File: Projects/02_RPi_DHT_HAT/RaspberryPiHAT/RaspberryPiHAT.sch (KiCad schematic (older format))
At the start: 0 parts

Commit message: Project 2: Add symbols from parts.md to Eeschema
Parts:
- added D?: D, symbol Device:D
- added J?: Raspberry_Pi_2_3, symbol Connector:Raspberry_Pi_2_3
- added R? (x3): R, symbol Device:R
- added SW?: SW_DPST, symbol Switch:SW_DPST
- added U?: DHT22, Sensor:Aosong_DHT11_5.5x12.0_P2.54mm, symbol Sensor:DHT11
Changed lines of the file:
@@
 Comment4 ""
 $EndDescr
+$Comp
+L Connector:Raspberry_Pi_2_3 J?
+U 1 1 61CF6995
+P 5550 3750
+F 0 "J?" H 5550 5231 50  0000 C CNN
+F 1 "Raspberry_Pi_2_3" H 5550 5140 50  0000 C CNN
+F 2 "" H 5550 3750 50  0001 C CNN
+F 3 "https://www.raspberrypi.org/documentation/hardware/raspberrypi/schematics/rpi_SCH_3bplus_1p0_reduced.pdf" H 5550 3750 50  0001 C CNN
+	1    5550 3750
+	1    0    0    -1
+$EndComp
+$Comp
+L Device:R R?
+U 1 1 61CFAE04
+P 3850 3000
+F 0 "R?" H 3920 3046 50  0000 L CNN
+F 1 "R" H 3920 2955 50  0000 L CNN
+F 2 "" V 3780 3000 50  0001 C CNN
+F 3 "~" H 3850 3000 50  0001 C CNN
+	1    3850 3000
+	1    0    0    -1
+$EndComp
+$Comp
+L Device:R R?
+U 1 1 61CFD123
+P 3850 3450
+F 0 "R?" H 3920 3496 50  0000 L CNN
+F 1 "R" H 3920 3405 50  0000 L CNN
+F 2 "" V 3780 3450 50  0001 C CNN
+F 3 "~" H 3850 3450 50  0001 C CNN
+	1    3850 3450
+	1    0    0    -1
+$EndComp
+$Comp
+L Sensor:DHT11 U?
+U 1 1 61CFDA18
+P 3850 4250
+F 0 "U?" H 3606 4296 50  0000 R CNN
+F 1 "DHT22" H 3606 4205 50  0000 R CNN
+F 2 "Sensor:Aosong_DHT11_5.5x12.0_P2.54mm" H 3850 3850 50  0001 C CNN
+F 3 "http://akizukidenshi.com/download/ds/aosong/DHT11.pdf" H 4000 4500 50  0001 C CNN
+	1    3850 4250
+	1    0    0    -1
+$EndComp
+$Comp
+L Device:D D?
+U 1 1 61CFE829
+P 3850 2450
+F 0 "D?" H 3850 2667 50  0000 C CNN
+F 1 "D" H 3850 2576 50  0000 C CNN
+F 2 "" H 3850 2450 50  0001 C CNN
+F 3 "~" H 3850 2450 50  0001 C CNN
+	1    3850 2450
+	1    0    0    -1
+$EndComp
+$Comp
+L Device:R R?
+U 1 1 61CFF65D
+P 7350 3550
+F 0 "R?" H 7420 3596 50  0000 L CNN
+F 1 "R" H 7420 3505 50  0000 L CNN
+F 2 "" V 7280 3550 50  0001 C CNN
+F 3 "~" H 7350 3550 50  0001 C CNN
+	1    7350 3550
+	1    0    0    -1
+$EndComp
+$Comp
+L Switch:SW_DPST SW?
+U 1 1 61D01499
+P 7350 2900
+F 0 "SW?" H 7350 3225 50  0000 C CNN
+F 1 "SW_DPST" H 7350 3134 50  0000 C CNN
+F 2 "" H 7350 2900 50  0001 C CNN
+F 3 "~" H 7350 2900 50  0001 C CNN
+	1    7350 2900
+	1    0    0    -1
+$EndComp
 $EndSCHEMATC

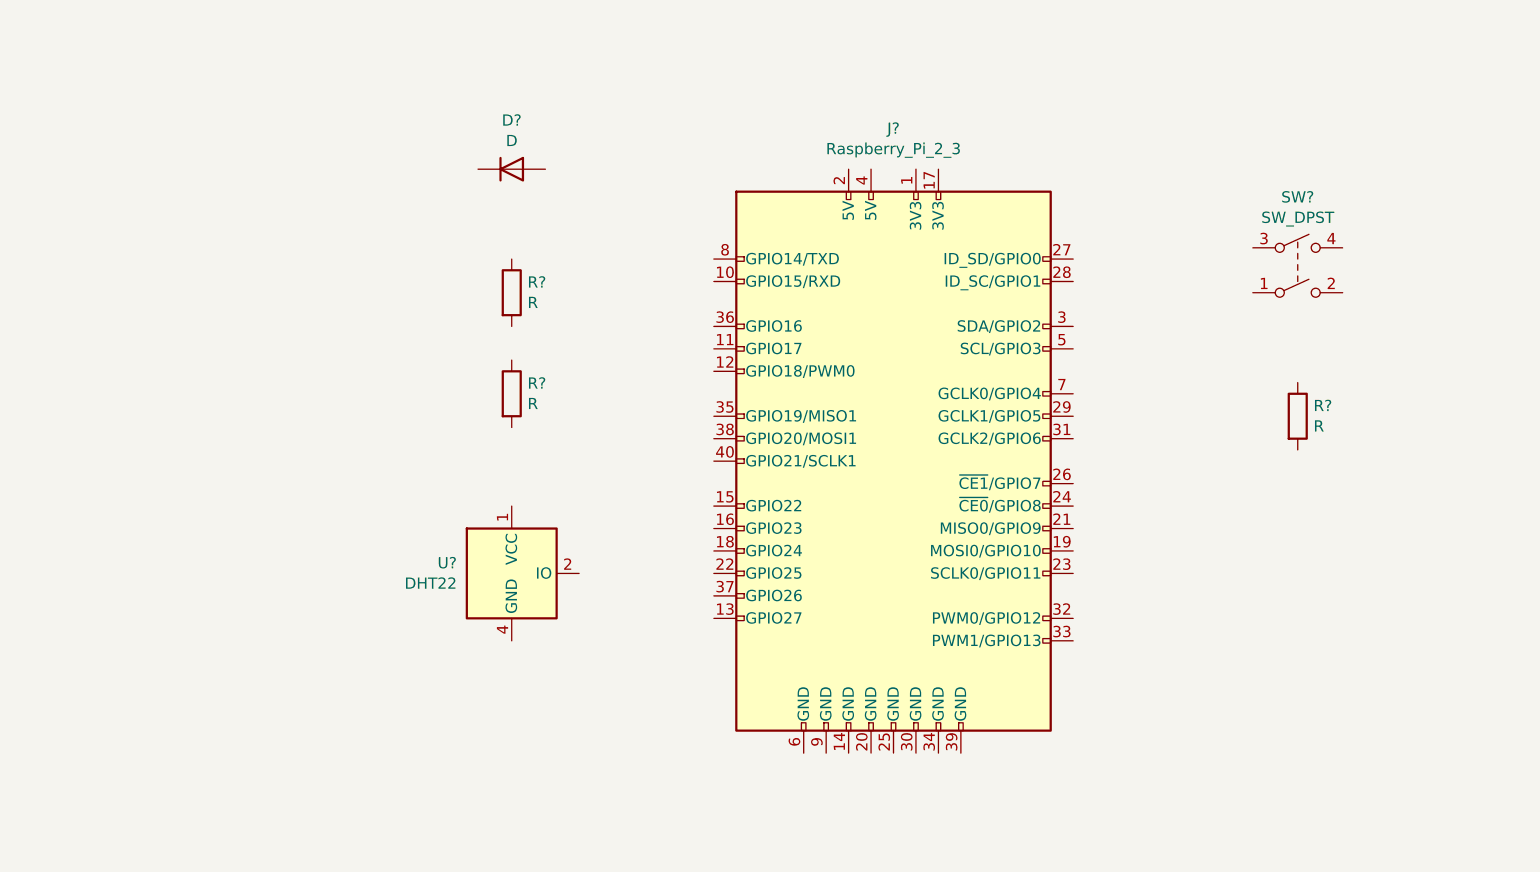
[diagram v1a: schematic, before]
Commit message: Project 2: Arrange, annotate, and associate Eeschema with footprints
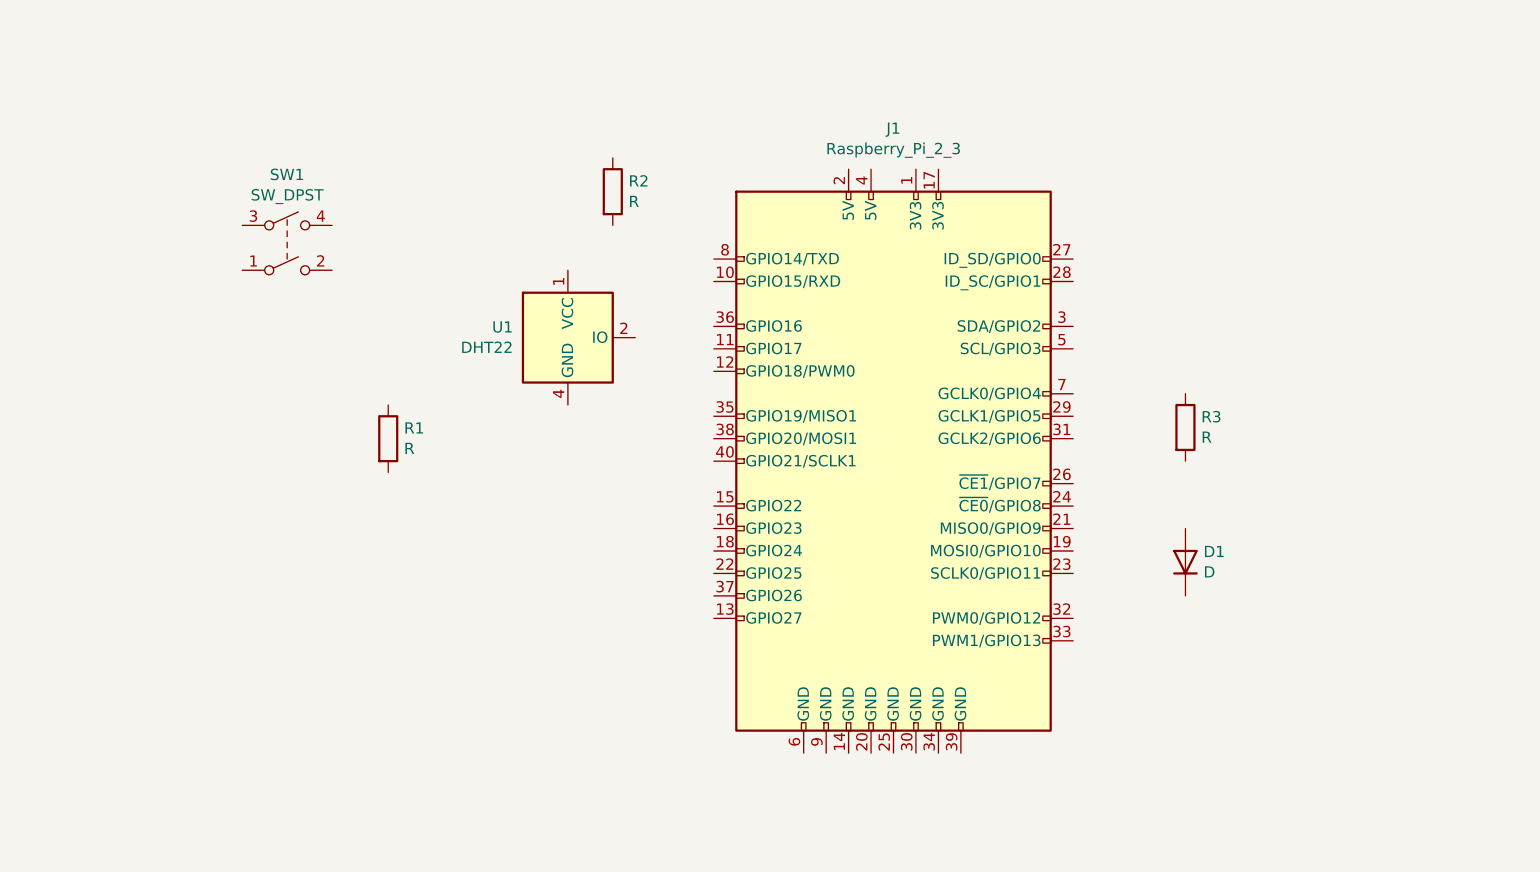
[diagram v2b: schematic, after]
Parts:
- D1: renamed from D?; footprint (none) -> LED_SMD:LED_0805_2012Metric
- J1: renamed from J?; footprint (none) -> Connector_PinSocket_2.54mm:PinSocket_2x08_P2.54mm_Vertical
- R1, R2, R3: renamed from R?; footprint (none) -> Resistor_SMD:R_0805_2012Metric
- SW1: renamed from SW?; footprint (none) -> freetronics_footprints:SW_PUSHBUTTON_PTH
- gave numbers to parts that had none: 1
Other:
- moved on the sheet: D1, R1, R2, R3, SW1, U1
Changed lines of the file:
@@
 $EndDescr
 $Comp
-L Connector:Raspberry_Pi_2_3 J?
+L Connector:Raspberry_Pi_2_3 J1
 U 1 1 61CF6995
 P 5550 3750
-F 0 "J?" H 5550 5231 50  0000 C CNN
+F 0 "J1" H 5550 5231 50  0000 C CNN
 F 1 "Raspberry_Pi_2_3" H 5550 5140 50  0000 C CNN
-F 2 "" H 5550 3750 50  0001 C CNN
+F 2 "Connector_PinSocket_2.54mm:PinSocket_2x08_P2.54mm_Vertical" H 5550 3750 50  0001 C CNN
 F 3 "https://www.raspberrypi.org/documentation/hardware/raspberrypi/schematics/rpi_SCH_3bplus_1p0_reduced.pdf" H 5550 3750 50  0001 C CNN
 	1    5550 3750
@@
 $EndComp
 $Comp
-L Device:R R?
+L Device:R R2
 U 1 1 61CFAE04
-P 3850 3000
-F 0 "R?" H 3920 3046 50  0000 L CNN
-F 1 "R" H 3920 2955 50  0000 L CNN
-F 2 "" V 3780 3000 50  0001 C CNN
-F 3 "~" H 3850 3000 50  0001 C CNN
-	1    3850 3000
+P 4300 2550
+F 0 "R2" H 4370 2596 50  0000 L CNN
+F 1 "R" H 4370 2505 50  0000 L CNN
+F 2 "Resistor_SMD:R_0805_2012Metric" V 4230 2550 50  0001 C CNN
+F 3 "~" H 4300 2550 50  0001 C CNN
+	1    4300 2550
 	1    0    0    -1
 $EndComp
 $Comp
-L Device:R R?
+L Device:R R3
 U 1 1 61CFD123
-P 3850 3450
-F 0 "R?" H 3920 3496 50  0000 L CNN
-F 1 "R" H 3920 3405 50  0000 L CNN
-F 2 "" V 3780 3450 50  0001 C CNN
-F 3 "~" H 3850 3450 50  0001 C CNN
-	1    3850 3450
+P 6850 3600
+F 0 "R3" H 6920 3646 50  0000 L CNN
+F 1 "R" H 6920 3555 50  0000 L CNN
+F 2 "Resistor_SMD:R_0805_2012Metric" V 6780 3600 50  0001 C CNN
+F 3 "~" H 6850 3600 50  0001 C CNN
+	1    6850 3600
 	1    0    0    -1
 $EndComp
 $Comp
-L Sensor:DHT11 U?
+L Sensor:DHT11 U1
 U 1 1 61CFDA18
-P 3850 4250
-F 0 "U?" H 3606 4296 50  0000 R CNN
-F 1 "DHT22" H 3606 4205 50  0000 R CNN
-F 2 "Sensor:Aosong_DHT11_5.5x12.0_P2.54mm" H 3850 3850 50  0001 C CNN
-F 3 "http://akizukidenshi.com/download/ds/aosong/DHT11.pdf" H 4000 4500 50  0001 C CNN
-	1    3850 4250
+P 4100 3200
+F 0 "U1" H 3856 3246 50  0000 R CNN
+F 1 "DHT22" H 3856 3155 50  0000 R CNN
+F 2 "Sensor:Aosong_DHT11_5.5x12.0_P2.54mm" H 4100 2800 50  0001 C CNN
+F 3 "http://akizukidenshi.com/download/ds/aosong/DHT11.pdf" H 4250 3450 50  0001 C CNN
+	1    4100 3200
 	1    0    0    -1
 $EndComp
 $Comp
-L Device:D D?
+L Device:D D1
 U 1 1 61CFE829
-P 3850 2450
-F 0 "D?" H 3850 2667 50  0000 C CNN
-F 1 "D" H 3850 2576 50  0000 C CNN
-F 2 "" H 3850 2450 50  0001 C CNN
-F 3 "~" H 3850 2450 50  0001 C CNN
-	1    3850 2450
+P 6850 4200
+F 0 "D1" V 6896 4120 50  0000 R CNN
+F 1 "D" V 6805 4120 50  0000 R CNN
+F 2 "LED_SMD:LED_0805_2012Metric" H 6850 4200 50  0001 C CNN
+F 3 "~" H 6850 4200 50  0001 C CNN
+	1    6850 4200
+	0    -1   -1   0
+$EndComp
+$Comp
+L Device:R R1
+U 1 1 61CFF65D
+P 3300 3650
+F 0 "R1" H 3370 3696 50  0000 L CNN
+F 1 "R" H 3370 3605 50  0000 L CNN
+F 2 "Resistor_SMD:R_0805_2012Metric" V 3230 3650 50  0001 C CNN
+F 3 "~" H 3300 3650 50  0001 C CNN
+	1    3300 3650
 	1    0    0    -1
 $EndComp
 $Comp
-L Device:R R?
-U 1 1 61CFF65D
-P 7350 3550
-F 0 "R?" H 7420 3596 50  0000 L CNN
-F 1 "R" H 7420 3505 50  0000 L CNN
-F 2 "" V 7280 3550 50  0001 C CNN
-F 3 "~" H 7350 3550 50  0001 C CNN
-	1    7350 3550
+L Switch:SW_DPST SW1
+U 1 1 61D01499
+P 2850 2800
+F 0 "SW1" H 2850 3125 50  0000 C CNN
+F 1 "SW_DPST" H 2850 3034 50  0000 C CNN
+F 2 "freetronics_footprints:SW_PUSHBUTTON_PTH" H 2850 2800 50  0001 C CNN
+F 3 "~" H 2850 2800 50  0001 C CNN
+	1    2850 2800
 	1    0    0    -1
 $EndComp
-$Comp
-L Switch:SW_DPST SW?
-U 1 1 61D01499
-P 7350 2900
-F 0 "SW?" H 7350 3225 50  0000 C CNN
-F 1 "SW_DPST" H 7350 3134 50  0000 C CNN
-F 2 "" H 7350 2900 50  0001 C CNN
-F 3 "~" H 7350 2900 50  0001 C CNN
-	1    7350 2900
-	1    0    0    -1
-$EndComp

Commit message: Project 2: Wire signals and power (PWR_FLAG)
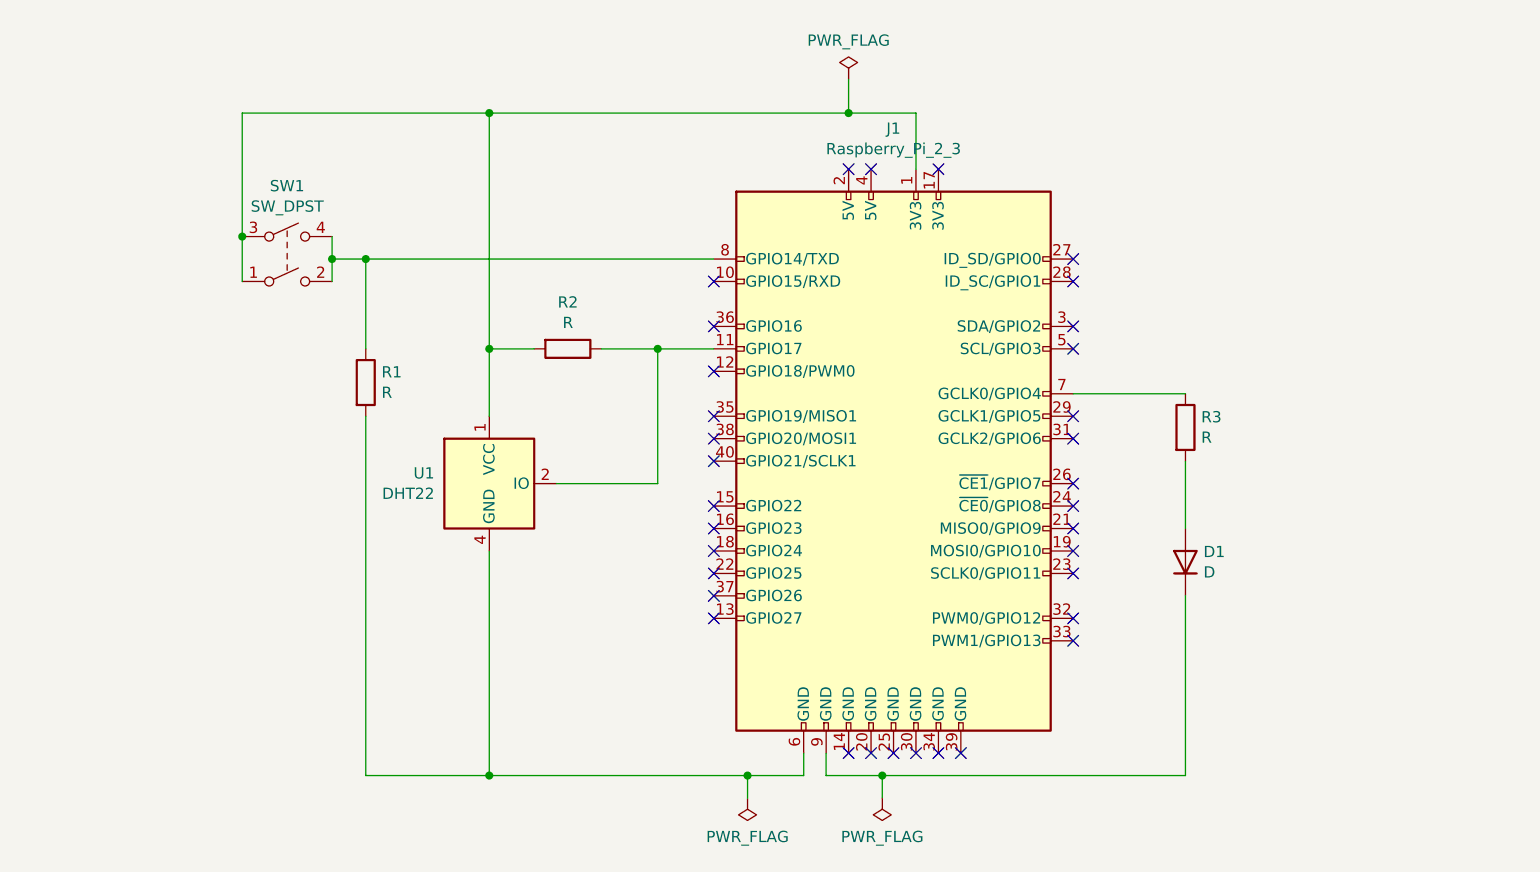
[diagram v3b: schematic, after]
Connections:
- net at J1.1 (3V3): now also R2.2, SW1.1, SW1.3, U1.1 (VCC)
- net at J1.11 (GPIO17): now also R2.1, U1.2 (IO)
- net at J1.6 (GND): now also R1.2, U1.4 (GND)
- net at J1.7 (GCLK0/GPIO4): now also R3.1
- net at J1.8 (GPIO14/TXD): now also R1.1, SW1.2, SW1.4
- net at J1.9 (GND): now also D1.1 (K)
- net at R3.2: now also D1.2 (A)
- no-connect marks 0 -> 34
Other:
- moved on the sheet: R1, R2, SW1, U1
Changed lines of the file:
@@
 $EndDescr
-$Comp
-L Connector:Raspberry_Pi_2_3 J1
-U 1 1 61CF6995
-P 5550 3750
-F 0 "J1" H 5550 5231 50  0000 C CNN
-F 1 "Raspberry_Pi_2_3" H 5550 5140 50  0000 C CNN
-F 2 "Connector_PinSocket_2.54mm:PinSocket_2x08_P2.54mm_Vertical" H 5550 3750 50  0001 C CNN
-F 3 "https://www.raspberrypi.org/documentation/hardware/raspberrypi/schematics/rpi_SCH_3bplus_1p0_reduced.pdf" H 5550 3750 50  0001 C CNN
-	1    5550 3750
-	1    0    0    -1
-$EndComp
-$Comp
-L Device:R R2
-U 1 1 61CFAE04
-P 4300 2550
-F 0 "R2" H 4370 2596 50  0000 L CNN
-F 1 "R" H 4370 2505 50  0000 L CNN
-F 2 "Resistor_SMD:R_0805_2012Metric" V 4230 2550 50  0001 C CNN
-F 3 "~" H 4300 2550 50  0001 C CNN
-	1    4300 2550
-	1    0    0    -1
-$EndComp
 $Comp
 L Device:R R3
@@
 L Sensor:DHT11 U1
 U 1 1 61CFDA18
-P 4100 3200
-F 0 "U1" H 3856 3246 50  0000 R CNN
-F 1 "DHT22" H 3856 3155 50  0000 R CNN
-F 2 "Sensor:Aosong_DHT11_5.5x12.0_P2.54mm" H 4100 2800 50  0001 C CNN
-F 3 "http://akizukidenshi.com/download/ds/aosong/DHT11.pdf" H 4250 3450 50  0001 C CNN
-	1    4100 3200
+P 3750 3850
+F 0 "U1" H 3506 3896 50  0000 R CNN
+F 1 "DHT22" H 3506 3805 50  0000 R CNN
+F 2 "Sensor:Aosong_DHT11_5.5x12.0_P2.54mm" H 3750 3450 50  0001 C CNN
+F 3 "http://akizukidenshi.com/download/ds/aosong/DHT11.pdf" H 3900 4100 50  0001 C CNN
+	1    3750 3850
 	1    0    0    -1
 $EndComp
@@
 L Device:R R1
 U 1 1 61CFF65D
-P 3300 3650
-F 0 "R1" H 3370 3696 50  0000 L CNN
-F 1 "R" H 3370 3605 50  0000 L CNN
-F 2 "Resistor_SMD:R_0805_2012Metric" V 3230 3650 50  0001 C CNN
-F 3 "~" H 3300 3650 50  0001 C CNN
-	1    3300 3650
+P 3200 3400
+F 0 "R1" H 3270 3446 50  0000 L CNN
+F 1 "R" H 3270 3355 50  0000 L CNN
+F 2 "Resistor_SMD:R_0805_2012Metric" V 3130 3400 50  0001 C CNN
+F 3 "~" H 3200 3400 50  0001 C CNN
+	1    3200 3400
 	1    0    0    -1
 $EndComp
@@
 L Switch:SW_DPST SW1
 U 1 1 61D01499
-P 2850 2800
-F 0 "SW1" H 2850 3125 50  0000 C CNN
-F 1 "SW_DPST" H 2850 3034 50  0000 C CNN
-F 2 "freetronics_footprints:SW_PUSHBUTTON_PTH" H 2850 2800 50  0001 C CNN
-F 3 "~" H 2850 2800 50  0001 C CNN
-	1    2850 2800
-	1    0    0    -1
-$EndComp
+P 2850 2850
+F 0 "SW1" H 2850 3175 50  0000 C CNN
+F 1 "SW_DPST" H 2850 3084 50  0000 C CNN
+F 2 "freetronics_footprints:SW_PUSHBUTTON_PTH" H 2850 2850 50  0001 C CNN
+F 3 "~" H 2850 2850 50  0001 C CNN
+	1    2850 2850
+	1    0    0    -1
+$EndComp
+Wire Wire Line
+	6850 3450 6350 3450
+Wire Wire Line
+	6850 4350 6850 5150
+Wire Wire Line
+	5250 5150 5250 5050
+Wire Wire Line
+	6850 4050 6850 3750
+$Comp
+L Connector:Raspberry_Pi_2_3 J1
+U 1 1 61CF6995
+P 5550 3750
+F 0 "J1" H 5550 5231 50  0000 C CNN
+F 1 "Raspberry_Pi_2_3" H 5550 5140 50  0000 C CNN
+F 2 "Connector_PinSocket_2.54mm:PinSocket_2x08_P2.54mm_Vertical" H 5550 3750 50  0001 C CNN
+F 3 "https://www.raspberrypi.org/documentation/hardware/raspberrypi/schematics/rpi_SCH_3bplus_1p0_reduced.pdf" H 5550 3750 50  0001 C CNN
+	1    5550 3750
+	1    0    0    -1
+$EndComp
+Wire Wire Line
+	5650 2450 5650 2200
+$Comp
+L Device:R R2
+U 1 1 61CFAE04
+P 4100 3250
+F 0 "R2" V 3893 3250 50  0000 C CNN
+F 1 "R" V 3984 3250 50  0000 C CNN
+F 2 "Resistor_SMD:R_0805_2012Metric" V 4030 3250 50  0001 C CNN
+F 3 "~" H 4100 3250 50  0001 C CNN
+	1    4100 3250
+	0    1    1    0
+$EndComp
+Wire Wire Line
+	3950 3250 3750 3250
+Connection ~ 3750 3250
+Wire Wire Line
+	3750 3250 3750 3550
+Wire Wire Line
+	4250 3250 4500 3250
+Wire Wire Line
+	4500 3850 4500 3250
+Wire Wire Line
+	4050 3850 4500 3850
+Connection ~ 4500 3250
+Wire Wire Line
+	4500 3250 4750 3250
+Wire Wire Line
+	3050 2750 3050 2850
+Connection ~ 3050 2850
+Wire Wire Line
+	3050 2850 3050 2950
+Wire Wire Line
+	3050 2850 3200 2850
+Wire Wire Line
+	3200 3250 3200 2850
+Connection ~ 3200 2850
+Wire Wire Line
+	3200 2850 4750 2850
+Wire Wire Line
+	3200 3550 3200 5150
+Wire Wire Line
+	5150 5150 5150 5050
+Wire Wire Line
+	3750 4150 3750 5150
+Wire Wire Line
+	3200 5150 3750 5150
+Connection ~ 3750 5150
+Wire Wire Line
+	2650 2200 3750 2200
+Wire Wire Line
+	2650 2200 2650 2750
+Connection ~ 2650 2750
+Wire Wire Line
+	2650 2750 2650 2950
+Wire Wire Line
+	3750 2200 3750 3250
+Connection ~ 3750 2200
+Wire Wire Line
+	3750 2200 5350 2200
+NoConn ~ 4750 2950
+NoConn ~ 4750 3150
+NoConn ~ 4750 3350
+NoConn ~ 4750 3550
+NoConn ~ 4750 3650
+NoConn ~ 4750 3750
+NoConn ~ 4750 3950
+NoConn ~ 4750 4050
+NoConn ~ 4750 4150
+NoConn ~ 4750 4250
+NoConn ~ 4750 4350
+NoConn ~ 4750 4450
+NoConn ~ 5350 5050
+NoConn ~ 5450 5050
+NoConn ~ 5550 5050
+NoConn ~ 5650 5050
+NoConn ~ 5750 5050
+NoConn ~ 5850 5050
+NoConn ~ 6350 4550
+NoConn ~ 6350 4450
+NoConn ~ 6350 4250
+NoConn ~ 6350 4150
+NoConn ~ 6350 4050
+NoConn ~ 6350 3950
+NoConn ~ 6350 3850
+NoConn ~ 6350 3650
+NoConn ~ 6350 3550
+NoConn ~ 6350 3250
+NoConn ~ 6350 3150
+NoConn ~ 6350 2950
+NoConn ~ 6350 2850
+NoConn ~ 5750 2450
+NoConn ~ 5450 2450
+NoConn ~ 5350 2450
+$Comp
+L power:PWR_FLAG #FLG0101
+U 1 1 61D30DD8
+P 5350 2050
+F 0 "#FLG0101" H 5350 2125 50  0001 C CNN
+F 1 "PWR_FLAG" H 5350 2223 50  0000 C CNN
+F 2 "" H 5350 2050 50  0001 C CNN
+F 3 "~" H 5350 2050 50  0001 C CNN
+	1    5350 2050
+	1    0    0    -1
+$EndComp
+Wire Wire Line
+	5350 2050 5350 2200
+Connection ~ 5350 2200
+Wire Wire Line
+	5350 2200 5650 2200
+Wire Wire Line
+	3750 5150 4900 5150
+Wire Wire Line
+	5250 5150 5500 5150
+$Comp
+L power:PWR_FLAG #FLG0102
+U 1 1 61D3DF92
+P 4900 5250
+F 0 "#FLG0102" H 4900 5325 50  0001 C CNN
+F 1 "PWR_FLAG" H 4900 5423 50  0000 C CNN
+F 2 "" H 4900 5250 50  0001 C CNN
+F 3 "~" H 4900 5250 50  0001 C CNN
+	1    4900 5250
+	-1   0    0    1
+$EndComp
+Wire Wire Line
+	4900 5250 4900 5150
+Connection ~ 4900 5150
+Wire Wire Line
+	4900 5150 5150 5150
+$Comp
+L power:PWR_FLAG #FLG0103
+U 1 1 61D3EFF5
+P 5500 5250
+F 0 "#FLG0103" H 5500 5325 50  0001 C CNN
+F 1 "PWR_FLAG" H 5500 5423 50  0000 C CNN
+F 2 "" H 5500 5250 50  0001 C CNN
+F 3 "~" H 5500 5250 50  0001 C CNN
+	1    5500 5250
+	-1   0    0    1
+$EndComp
+Wire Wire Line
+	5500 5250 5500 5150
+Connection ~ 5500 5150
+Wire Wire Line
+	5500 5150 6850 5150
 $EndSCHEMATC
